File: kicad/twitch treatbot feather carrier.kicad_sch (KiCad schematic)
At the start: 0 parts

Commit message: PCB floorplanning
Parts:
- added A1: Adafruit_Feather_HUZZAH_ESP8266, Module:Adafruit_Feather, symbol MCU_Module:Adafruit_Feather_HUZZAH_ESP8266
- added C1: 1000u/25V, Capacitor_THT:CP_Radial_D13.0mm_P5.00mm, symbol Device:C_Polarized_Small_US
- added C2: 10u/25V, Capacitor_THT:CP_Radial_D8.0mm_P3.80mm, symbol Device:C_Polarized_Small_US
- added C3, C4, C7, C9: 10u, Capacitor_SMD:C_0805_2012Metric, symbol My Library:C_0805
- added C5: 1u, Capacitor_SMD:C_0805_2012Metric, symbol My Library:C_0805
- added D1: +12V, LED_SMD:LED_1206_3216Metric, symbol My Library:D_1206
- added D2: +5V, LED_SMD:LED_1206_3216Metric, symbol My Library:D_1206
- added D3: +3V3, LED_SMD:LED_1206_3216Metric, symbol My Library:D_1206
- added J1: 128x64 OLED, Connector_PinSocket_2.54mm:PinSocket_1x04_P2.54mm_Vertical, symbol Connector_Generic:Conn_01x04
- added J2: Quiic MP3 Trigger [CHECK FOOTPRINT], Connector_PinSocket_2.54mm:PinSocket_1x04_P2.54mm_Vertical, symbol Connector_Generic:Conn_01x04
- added J3: M2, TerminalBlock:TerminalBlock_Altech_AK300-2_P5.00mm, symbol Connector_Generic:Conn_01x02
- added J4: M1, TerminalBlock:TerminalBlock_Altech_AK300-2_P5.00mm, symbol Connector_Generic:Conn_01x02
- added J6: NEO_Signal, TerminalBlock:TerminalBlock_Altech_AK300-2_P5.00mm, symbol Connector_Generic:Conn_01x02
- added Q1: BSS138, Package_TO_SOT_SMD:SOT-23, symbol Transistor_FET:BSS138
- added R1, R4, R7: 10k, Resistor_SMD:R_0805_2012Metric, symbol My Library:R_0805
- added R2, RDNP1: 4k7, Resistor_SMD:R_0805_2012Metric, symbol My Library:R_0805
- added R3, R5, R6: 1k, Resistor_SMD:R_0805_2012Metric, symbol My Library:R_0805
- added SW1: ESP RESET, My Libraries:SW_Push_CK_PTS525_SM15, symbol Switch:SW_Push
- added SW2: Wiggle, My Libraries:SW_Push_CK_PTS525_SM15, symbol Switch:SW_Push
- added TP1: TestPoint_Harwin, My Libraries:Harwin-S1751-46-Test-Point, symbol My Library:TestPoint_Harwin
- added U1: TMC2208_BREAKOUT, My Libraries:DIP-16_W12.7mm, symbol My Library:TMC2208_BREAKOUT
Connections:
- new net: D1.1 (K), R3.1
- new net: A1.1 (~{RESET}), SW1.1
- new net: A1.24 (IO12/MISO), TP1.1
- new net: D3.1 (K), R6.1
- new net: D2.1 (K), R5.1
- new net +12V: C1.1, C2.1, D1.2 (A), U1.8 (VM)
- new net +3V3: A1.2 (3V3), C3.1, C5.1, D3.2 (A), Q1.1 (G), R2.2, R4.1, U1.2 (VIO)
- new net +5V: A1.26 (USB), A1.27 (EN), C4.1, C7.1, C9.1, D2.2 (A), R1.1, R7.1, RDNP1.1
- new net 3v3: J2.3 (Pin_3)
- new net 5V: J1.4 (Pin_4)
- new net GND: A1.4 (GND), C1.2, C2.2, C3.2, C4.2, C5.2, C7.2, C9.2, J1.3 (Pin_3), J2.4 (Pin_4), J6.2 (Pin_2), R1.2, R3.2, R5.2, R6.2, SW1.2, SW2.2, U1.1 (GND), U1.7 (GND)
- new net M1A: J4.1 (Pin_1), U1.5 (M1A)
- new net M1B: J4.2 (Pin_2), U1.6 (M1B)
- new net M2A: J3.2 (Pin_2), U1.4 (M2A)
- new net M2B: J3.1 (Pin_1), U1.3 (M2B)
- new net NEO_3v: A1.11 (SCK/IO14), Q1.2 (S), R4.2
- new net NEO_5v: J6.1 (Pin_1), Q1.3 (D), R7.2
- new net SCL: A1.18 (SCL/IO5), J1.2 (Pin_2), J2.1 (Pin_1)
- new net SDA: A1.17 (SDA/IO4), J1.1 (Pin_1), J2.2 (Pin_2)
- new net STEP_DIR: A1.20 (IO16), U1.16 (DIR)
- new net STEP_EN: A1.19 (IO2), R2.1, U1.9 (EN)
- new net STEP_STEP: A1.22 (IO15), U1.15 (STEP)
- new net Wiggle: A1.23 (IO13/MOSI), RDNP1.2, SW2.1
- no-connect marks 0 -> 13
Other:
- note added: "5V Consumers: Huzzah Module NeoPixels"
- note added: "I2C: 0x37"
- note added: "I2C: 0x3C"
- note added: "M2B - Green M2A - Brown M1A - Red M1B - Yellow"
- note added: "Move STEP signal from IO0 to IO15. IO0 should have an on-board led"

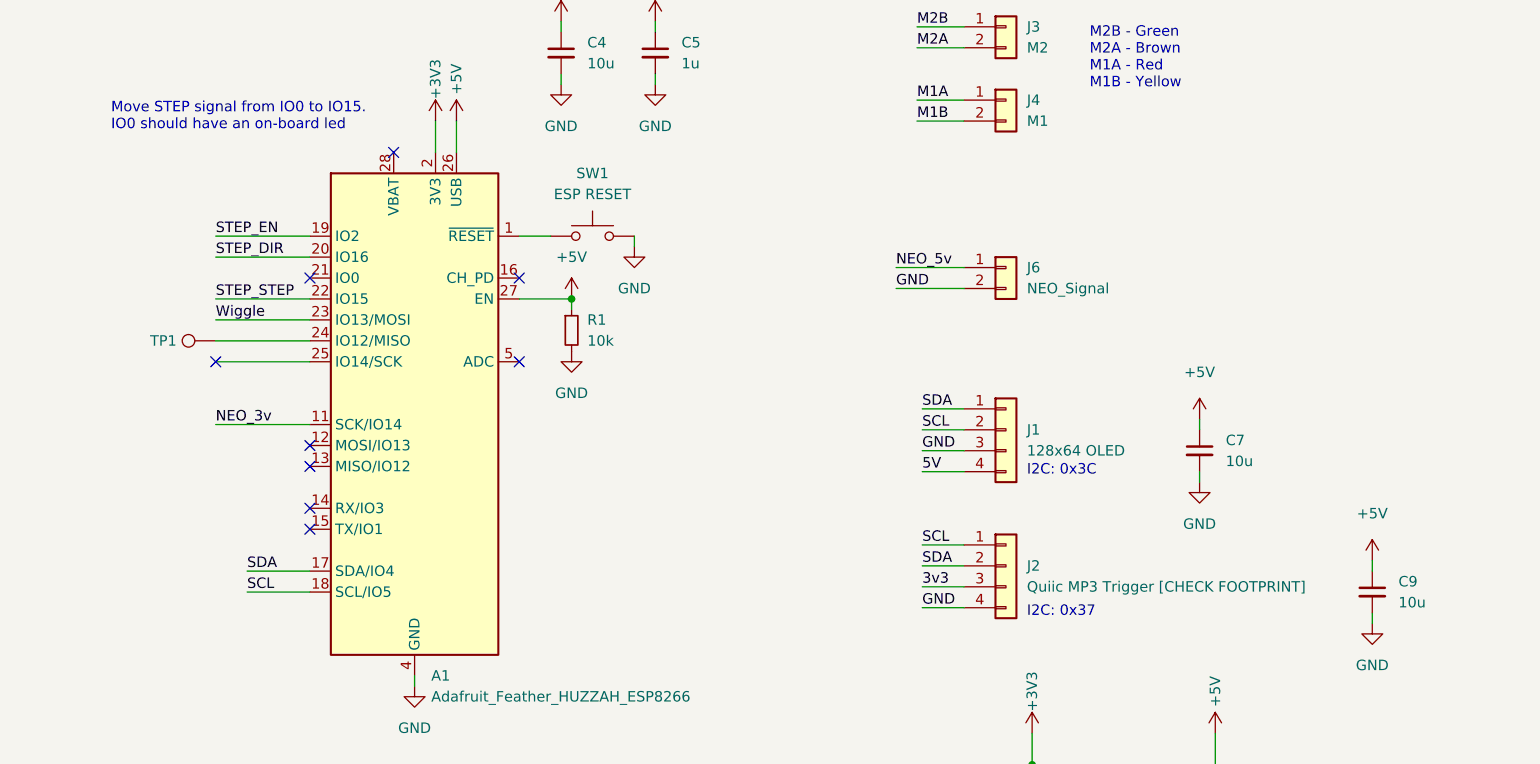
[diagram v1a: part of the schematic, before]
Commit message: first floorplan done
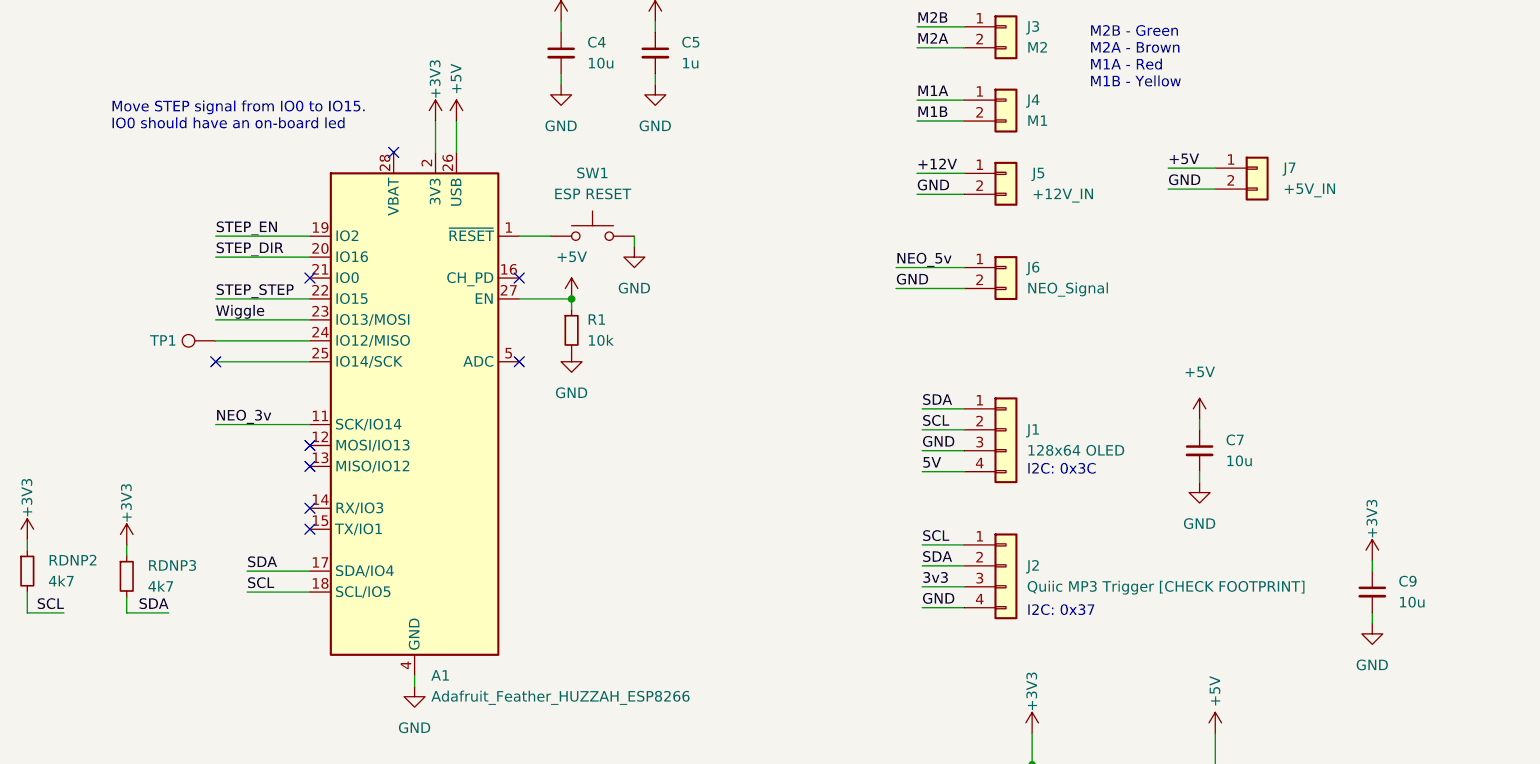
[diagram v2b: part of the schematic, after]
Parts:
- added J5: +12V_IN, TerminalBlock:TerminalBlock_Altech_AK300-2_P5.00mm, symbol Connector_Generic:Conn_01x02
- added J7: +5V_IN, Connector_PinHeader_2.54mm:PinHeader_1x02_P2.54mm_Vertical, symbol Connector_Generic:Conn_01x02
- added RDNP2, RDNP3: 4k7, Resistor_SMD:R_0805_2012Metric, symbol My Library:R_0805
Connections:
- net +12V: now also J5.1 (Pin_1)
- net +3V3: now also C9.1, RDNP2.1, RDNP3.1
- net +5V: now also J7.1 (Pin_1); no longer C9.1
- net GND: now also J5.2 (Pin_2), J7.2 (Pin_2)
- net SCL: now also RDNP2.2
- net SDA: now also RDNP3.2

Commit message: 2nd floorplan
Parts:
- removed TP1: TestPoint_Harwin, My Libraries:Harwin-S1751-46-Test-Point, symbol My Library:TestPoint_Harwin
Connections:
- net NEO_3v: now also A1.15 (TX/IO1); no longer A1.11 (SCK/IO14)
- net STEP_DIR: now also A1.11 (SCK/IO14); no longer A1.20 (IO16)
- net STEP_EN: now also A1.13 (MISO/IO12); no longer A1.19 (IO2)
- net STEP_STEP: now also A1.12 (MOSI/IO13); no longer A1.22 (IO15)
- net Wiggle: no longer A1.23 (IO13/MOSI)
- no-connect marks 13 -> 12
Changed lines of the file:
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@@
   )
   (no_connect (at 81.28 57.15))
-  (no_connect (at 44.45 67.31))
   (no_connect (at 81.28 67.31))
+  (no_connect (at 55.88 62.23))
+  (no_connect (at 55.88 64.77))
+  (no_connect (at 55.88 67.31))
   (no_connect (at 55.88 57.15))
   (no_connect (at 66.04 41.91))
-  (no_connect (at 55.88 80.01))
-  (no_connect (at 55.88 77.47))
   (no_connect (at 55.88 85.09))
-  (no_connect (at 55.88 87.63))
   (no_connect (at 111.76 141.605))
   (no_connect (at 111.76 139.065))
@@
     (stroke (width 0) (type default) (color 0 0 0 0))
   )
+  (wire (pts (xy 44.45 74.93) (xy 55.88 74.93))
+    (stroke (width 0) (type default) (color 0 0 0 0))
+  )
   (wire (pts (xy 100.965 175.895) (xy 100.965 174.625))
     (stroke (width 0) (type default) (color 0 0 0 0))
@@
     (stroke (width 0) (type default) (color 0 0 0 0))
   )
-  (wire (pts (xy 44.45 62.23) (xy 55.88 62.23))
+  (wire (pts (xy 44.45 80.01) (xy 55.88 80.01))
     (stroke (width 0) (type default) (color 0 0 0 0))
   )
@@
     (stroke (width 0) (type default) (color 0 0 0 0))
   )
-  (wire (pts (xy 44.45 74.93) (xy 55.88 74.93))
+  (wire (pts (xy 44.45 87.63) (xy 55.88 87.63))
     (stroke (width 0) (type default) (color 0 0 0 0))
   )
@@
     (stroke (width 0) (type default) (color 0 0 0 0))
   )
-  (wire (pts (xy 44.45 67.31) (xy 55.88 67.31))
-    (stroke (width 0) (type default) (color 0 0 0 0))
-  )
   (wire (pts (xy 73.66 141.605) (xy 83.82 141.605))
     (stroke (width 0) (type default) (color 0 0 0 0))
@@
     (stroke (width 0) (type default) (color 0 0 0 0))
   )
-  (wire (pts (xy 44.45 64.77) (xy 55.88 64.77))
+  (wire (pts (xy 44.45 77.47) (xy 55.88 77.47))
     (stroke (width 0) (type default) (color 0 0 0 0))
   )
@@
     (effects (font (size 1.27 1.27)) (justify left bottom))
   )
-  (label "STEP_DIR" (at 44.45 54.61 0)
+  (label "STEP_DIR" (at 44.45 74.93 0)
     (effects (font (size 1.27 1.27)) (justify left bottom))
   )
@@
     (effects (font (size 1.27 1.27)) (justify right bottom))
   )
-  (label "NEO_3v" (at 44.45 74.93 0)
+  (label "NEO_3v" (at 44.45 87.63 0)
     (effects (font (size 1.27 1.27)) (justify left bottom))
   )
@@
     (effects (font (size 1.27 1.27)) (justify left bottom))
   )
-  (label "STEP_EN" (at 44.45 52.07 0)
+  (label "STEP_EN" (at 44.45 80.01 0)
     (effects (font (size 1.27 1.27)) (justify left bottom))
   )
@@
     (effects (font (size 1.27 1.27)) (justify left bottom))
   )
-  (label "Wiggle" (at 44.45 62.23 0)
+  (label "Wiggle" (at 33.02 56.515 0)
     (effects (font (size 1.27 1.27)) (justify left bottom))
   )
@@
     (effects (font (size 1.27 1.27)) (justify right bottom))
   )
-  (label "STEP_STEP" (at 44.45 59.69 0)
+  (label "STEP_STEP" (at 44.45 77.47 0)
     (effects (font (size 1.27 1.27)) (justify left bottom))
   )
@@
     (pin "2")
   )
-  (symbol (lib_id "My Library:TestPoint_Harwin") (at 44.45 64.77 90) (unit 1)
-    (in_bom yes) (on_board yes)
-    (property "Reference" "TP1" (id 0) (at 38.1 64.77 90))
-    (property "Value" "TestPoint_Harwin" (id 1) (at 39.37 64.77 0)
-      (effects (font (size 1.27 1.27)) hide)
-    )
-    (property "Footprint" "My Libraries:Harwin-S1751-46-Test-Point" (id 2) (at 44.45 59.69 0)
-      (effects (font (size 1.27 1.27)) hide)
-    )
-    (property "Datasheet" "~" (id 3) (at 44.45 59.69 0)
-      (effects (font (size 1.27 1.27)) hide)
-    )
-    (pin "1")
-  )
   (symbol (lib_id "My Library:R_0805") (at 152.4 176.53 0) (unit 1)
     (in_bom yes) (on_board yes) (fields_autoplaced)
@@
       (reference "SW2") (unit 1) (value "Wiggle") (footprint "My Libraries:SW_Push_CK_PTS525_SM15")
     )
-    (path "/a859030b-6af6-43a8-aaed-f301fe51e815"
-      (reference "TP1") (unit 1) (value "TestPoint_Harwin") (footprint "My Libraries:Harwin-S1751-46-Test-Point")
-    )
     (path "/af8a5b1c-8786-4ea2-ac85-5bb7e742c6ba"

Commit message: Layout done, fully routed, most of silk done, debating if to convert to 2 layer board
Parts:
- added TP1, TP2, TP3, TP4: TestPoint_Harwin, My Libraries:Harwin-S1751-46-Test-Point, symbol My Library:TestPoint_Harwin
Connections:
- net 3v3 is gone; now on net +3V3: J2.3 (Pin_3)
- net 5V is gone; now on net +5V: J1.4 (Pin_4)
- net +12V: now also J5.2 (Pin_2); no longer J5.1 (Pin_1)
- net GND: now also J5.1 (Pin_1), J6.1 (Pin_1), TP3.1, TP4.1; no longer J5.2 (Pin_2), J6.2 (Pin_2)
- net M1A: now also J4.2 (Pin_2); no longer J4.1 (Pin_1)
- net M1B: now also J4.1 (Pin_1); no longer J4.2 (Pin_2)
- net M2A: now also J3.1 (Pin_1); no longer J3.2 (Pin_2)
- net M2B: now also J3.2 (Pin_2); no longer J3.1 (Pin_1)
- net NEO_3v: now also TP1.1
- net NEO_5v: now also J6.2 (Pin_2), TP2.1; no longer J6.1 (Pin_1)
- net Wiggle: now also A1.22 (IO15)
- net ~{RESET}: now reaches A1.1 (~{RESET}), SW1.1

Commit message: forgot mounting holes!
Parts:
- added H1, H2, H3, H4: MountingHole, MountingHole:MountingHole_2.2mm_M2, symbol Mechanical:MountingHole
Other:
- note removed: "5V Consumers: Huzzah Module NeoPixels"
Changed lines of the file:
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@@
     (stroke (width 0) (type default) (color 0 0 0 0))
-  )
-  (text "5V Consumers:\nHuzzah Module\nNeoPixels" (at 254 39.37 0)
-    (effects (font (size 1.27 1.27)) (justify left bottom))
   )
   (text "Move STEP signal from IO0 to IO15.\nIO0 should have an on-board led"
@@
   (symbol (lib_id "power:+3V3") (at 130.175 94.615 90) (unit 1)
     (in_bom yes) (on_board yes)
-    (property "Reference" "#PWR?" (id 0) (at 133.985 94.615 0)
+    (property "Reference" "#PWR0138" (id 0) (at 133.985 94.615 0)
       (effects (font (size 1.27 1.27)) hide)
     )
@@
     )
     (pin "1")
+  )
+  (symbol (lib_id "Mechanical:MountingHole") (at 248.92 113.03 0) (unit 1)
+    (in_bom yes) (on_board yes) (fields_autoplaced)
+    (property "Reference" "H1" (id 0) (at 251.46 111.7599 0)
+      (effects (font (size 1.27 1.27)) (justify left))
+    )
+    (property "Value" "MountingHole" (id 1) (at 251.46 114.2999 0)
+      (effects (font (size 1.27 1.27)) (justify left))
+    )
+    (property "Footprint" "MountingHole:MountingHole_2.2mm_M2" (id 2) (at 248.92 113.03 0)
+      (effects (font (size 1.27 1.27)) hide)
+    )
+    (property "Datasheet" "~" (id 3) (at 248.92 113.03 0)
+      (effects (font (size 1.27 1.27)) hide)
+    )
+  )
+  (symbol (lib_id "Mechanical:MountingHole") (at 248.92 123.19 0) (unit 1)
+    (in_bom yes) (on_board yes) (fields_autoplaced)
+    (property "Reference" "H3" (id 0) (at 251.46 121.9199 0)
+      (effects (font (size 1.27 1.27)) (justify left))
+    )
+    (property "Value" "MountingHole" (id 1) (at 251.46 124.4599 0)
+      (effects (font (size 1.27 1.27)) (justify left))
+    )
+    (property "Footprint" "MountingHole:MountingHole_2.2mm_M2" (id 2) (at 248.92 123.19 0)
+      (effects (font (size 1.27 1.27)) hide)
+    )
+    (property "Datasheet" "~" (id 3) (at 248.92 123.19 0)
+      (effects (font (size 1.27 1.27)) hide)
+    )
   )
   (symbol (lib_id "MCU_Module:Adafruit_Feather_HUZZAH_ESP8266") (at 68.58 72.39 0) (unit 1)
@@
   (symbol (lib_id "power:+5V") (at 130.175 80.645 90) (unit 1)
     (in_bom yes) (on_board yes)
-    (property "Reference" "#PWR?" (id 0) (at 133.985 80.645 0)
+    (property "Reference" "#PWR0139" (id 0) (at 133.985 80.645 0)
       (effects (font (size 1.27 1.27)) hide)
     )
@@
     (pin "1")
     (pin "2")
+  )
+  (symbol (lib_id "Mechanical:MountingHole") (at 248.92 128.27 0) (unit 1)
+    (in_bom yes) (on_board yes) (fields_autoplaced)
+    (property "Reference" "H4" (id 0) (at 251.46 126.9999 0)
+      (effects (font (size 1.27 1.27)) (justify left))
+    )
+    (property "Value" "MountingHole" (id 1) (at 251.46 129.5399 0)
+      (effects (font (size 1.27 1.27)) (justify left))
+    )
+    (property "Footprint" "MountingHole:MountingHole_2.2mm_M2" (id 2) (at 248.92 128.27 0)
+      (effects (font (size 1.27 1.27)) hide)
+    )
+    (property "Datasheet" "~" (id 3) (at 248.92 128.27 0)
+      (effects (font (size 1.27 1.27)) hide)
+    )
   )
   (symbol (lib_id "power:+3V3") (at 71.12 38.1 0) (unit 1)
@@
     (pin "2")
   )
+  (symbol (lib_id "Mechanical:MountingHole") (at 248.92 118.11 0) (unit 1)
+    (in_bom yes) (on_board yes) (fields_autoplaced)
+    (property "Reference" "H2" (id 0) (at 251.46 116.8399 0)
+      (effects (font (size 1.27 1.27)) (justify left))
+    )
+    (property "Value" "MountingHole" (id 1) (at 251.46 119.3799 0)
+      (effects (font (size 1.27 1.27)) (justify left))
+    )
+    (property "Footprint" "MountingHole:MountingHole_2.2mm_M2" (id 2) (at 248.92 118.11 0)
+      (effects (font (size 1.27 1.27)) hide)
+    )
+    (property "Datasheet" "~" (id 3) (at 248.92 118.11 0)
+      (effects (font (size 1.27 1.27)) hide)
+    )
+  )
   (symbol (lib_id "power:+12V") (at 139.7 166.37 0) (unit 1)
     (in_bom yes) (on_board yes) (fields_autoplaced)
@@
     )
     (path "/37f288e8-5c6c-483f-9e71-5716f2c6ac87"
-      (reference "#PWR?") (unit 1) (value "+3V3") (footprint "")
+      (reference "#PWR0138") (unit 1) (value "+3V3") (footprint "")
     )
     (path "/6585a5c5-11aa-4caa-b3d3-d853650d5575"
-      (reference "#PWR?") (unit 1) (value "+5V") (footprint "")
+      (reference "#PWR0139") (unit 1) (value "+5V") (footprint "")
     )
     (path "/57121f1d-c971-4830-b974-00f7d706f0c9"
@@
       (reference "D3") (unit 1) (value "+3V3") (footprint "LED_SMD:LED_1206_3216Metric")
     )
+    (path "/551310a4-3882-4605-bfec-f0802df1435c"
+      (reference "H1") (unit 1) (value "MountingHole") (footprint "MountingHole:MountingHole_2.2mm_M2")
+    )
+    (path "/c6e87fd8-3786-4afc-bdfd-4fa8d3e76ad7"
+      (reference "H2") (unit 1) (value "MountingHole") (footprint "MountingHole:MountingHole_2.2mm_M2")
+    )
+    (path "/55f629e5-1c97-4453-a1ae-599ac25f2ed5"
+      (reference "H3") (unit 1) (value "MountingHole") (footprint "MountingHole:MountingHole_2.2mm_M2")
+    )
+    (path "/8326c248-4963-4df7-8949-20fc1935f203"
+      (reference "H4") (unit 1) (value "MountingHole") (footprint "MountingHole:MountingHole_2.2mm_M2")
+    )
     (path "/077c7713-5f8a-46ad-9e1e-0a158b076dfa"
